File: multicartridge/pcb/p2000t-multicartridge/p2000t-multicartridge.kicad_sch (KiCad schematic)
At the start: 20 parts, among them J1 P2000T_cartridge_edge, J2 DIPconn, SW1 Soft Reset, U1 SST39SF040, U2 74HC123, U3 74HC00

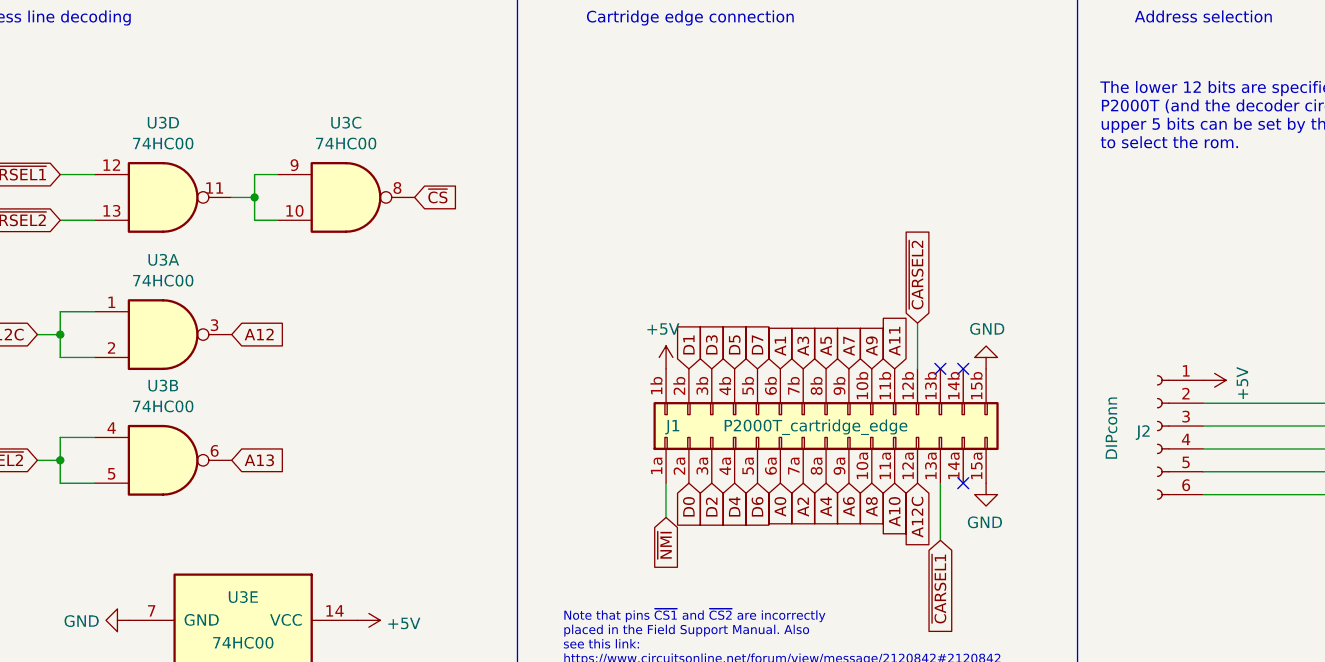
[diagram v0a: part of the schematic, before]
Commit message: Tuning lay-out multirom cartridge
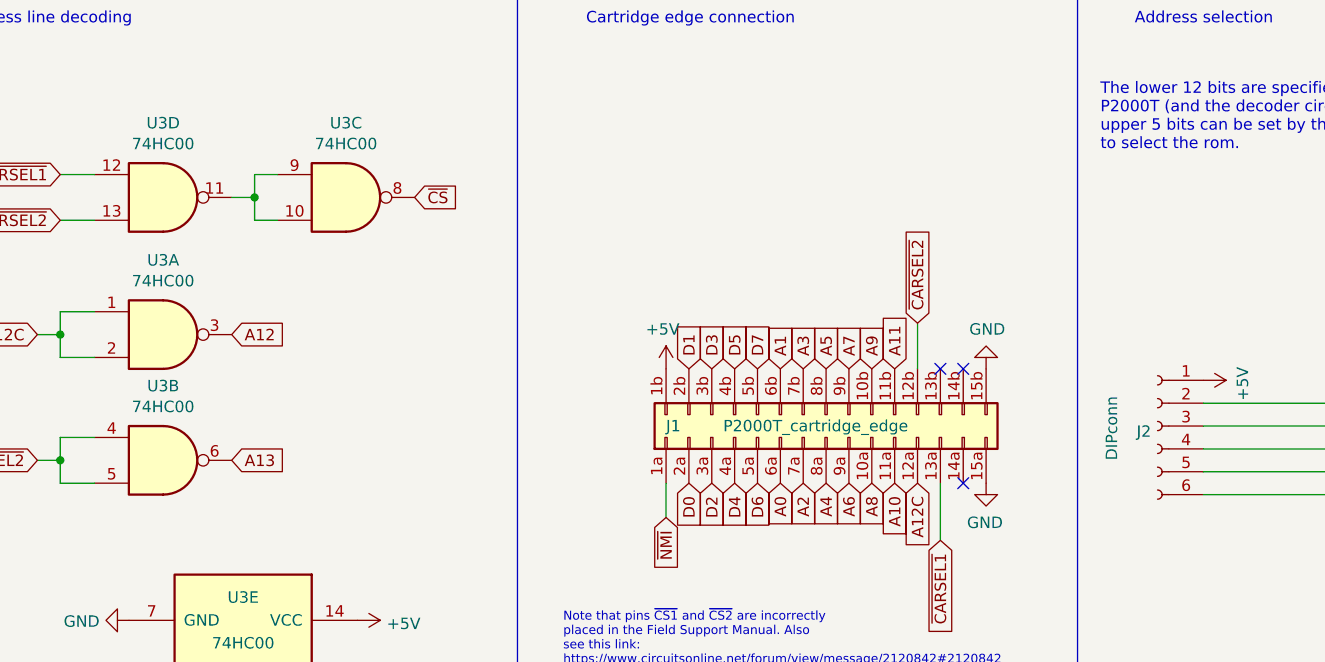
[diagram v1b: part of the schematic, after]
